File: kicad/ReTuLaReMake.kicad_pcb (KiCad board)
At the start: 2 copper layers, 54 x 26 mm, 23 parts, among them J1 40 Pin DIP Header, U1 ATF1508AS-10AU100

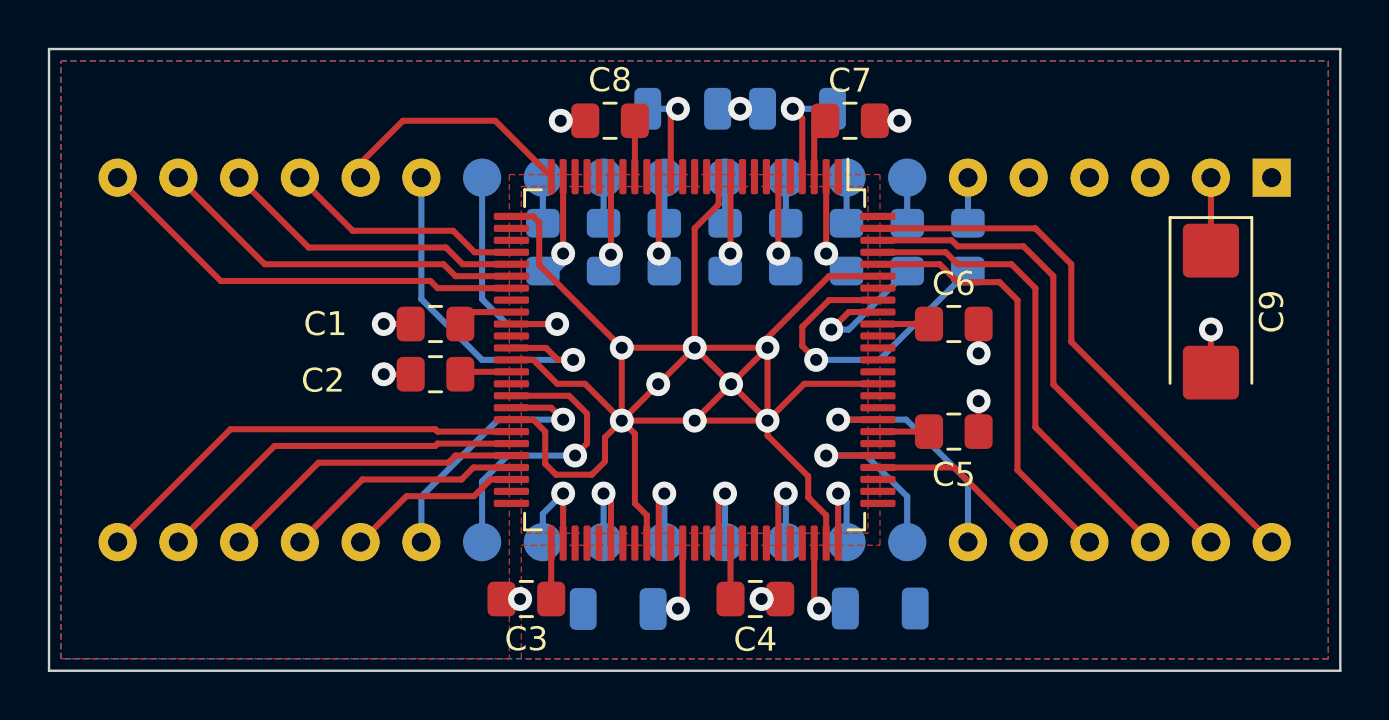
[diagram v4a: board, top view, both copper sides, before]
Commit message: KiCAD: Correct pin assignments to match JK's PCBs
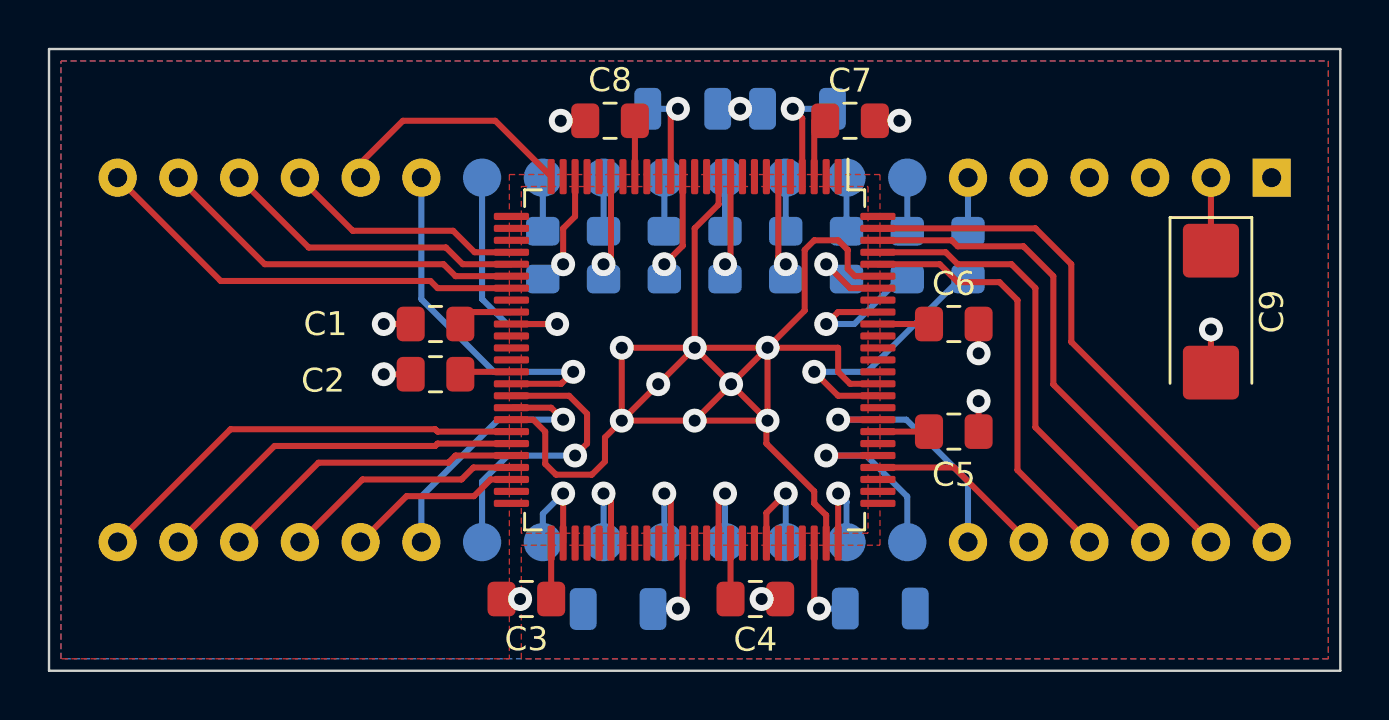
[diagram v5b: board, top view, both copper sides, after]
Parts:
- moved R1 0.33 mm to (138.4, 115.0)
- moved R2 0.33 mm to (135.9, 115.0)
- moved R3 0.33 mm to (133.3, 115.0)
- moved R4 0.33 mm to (130.8, 115.0)
- moved R5 0.33 mm to (128.3, 115.0)
- moved R6 0.33 mm to (125.7, 115.0)
- moved R7 0.33 mm to (123.2, 115.0)
- moved R8 0.33 mm to (120.7, 115.0)
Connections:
- U1 pad 14: unconnected-(U1-Pad14) -> /HD5
- U1 pad 16: /HD5 -> unconnected-(U1-Pad16)
- U1 pad 2: /HD2 -> unconnected-(U1-Pad2)
- U1 pad 23: unconnected-(U1-Pad23) -> /HD7
- U1 pad 24: /HD7 -> unconnected-(U1-Pad24)
- U1 pad 37: /HA1 -> unconnected-(U1-Pad37)
- U1 pad 40: unconnected-(U1-Pad40) -> /HA1
- U1 pad 60: /PD5 -> unconnected-(U1-Pad60)
- U1 pad 61: unconnected-(U1-Pad61) -> /PD5
- U1 pad 69: unconnected-(U1-Pad69) -> /PD3
- U1 pad 70: /PD3 -> unconnected-(U1-Pad70)
- U1 pad 85: unconnected-(U1-Pad85) -> /HD0
- U1 pad 93: /HD0 -> unconnected-(U1-Pad93)
- U1 pad 94: unconnected-(U1-Pad94) -> /HD2
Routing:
- net GND: track 93.8 -> 78.2 mm
- net /HD0: track 13.1 -> 10.8 mm
- net /HD7: track 4.08 -> 4.98 mm
- net /HD3: track 3.66 -> 4.41 mm
- net /HD6: track 3.70 -> 4.41 mm
- net /HD5: track 4.04 -> 4.60 mm

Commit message: KiCAD: Connect unused CPLD pins to GND
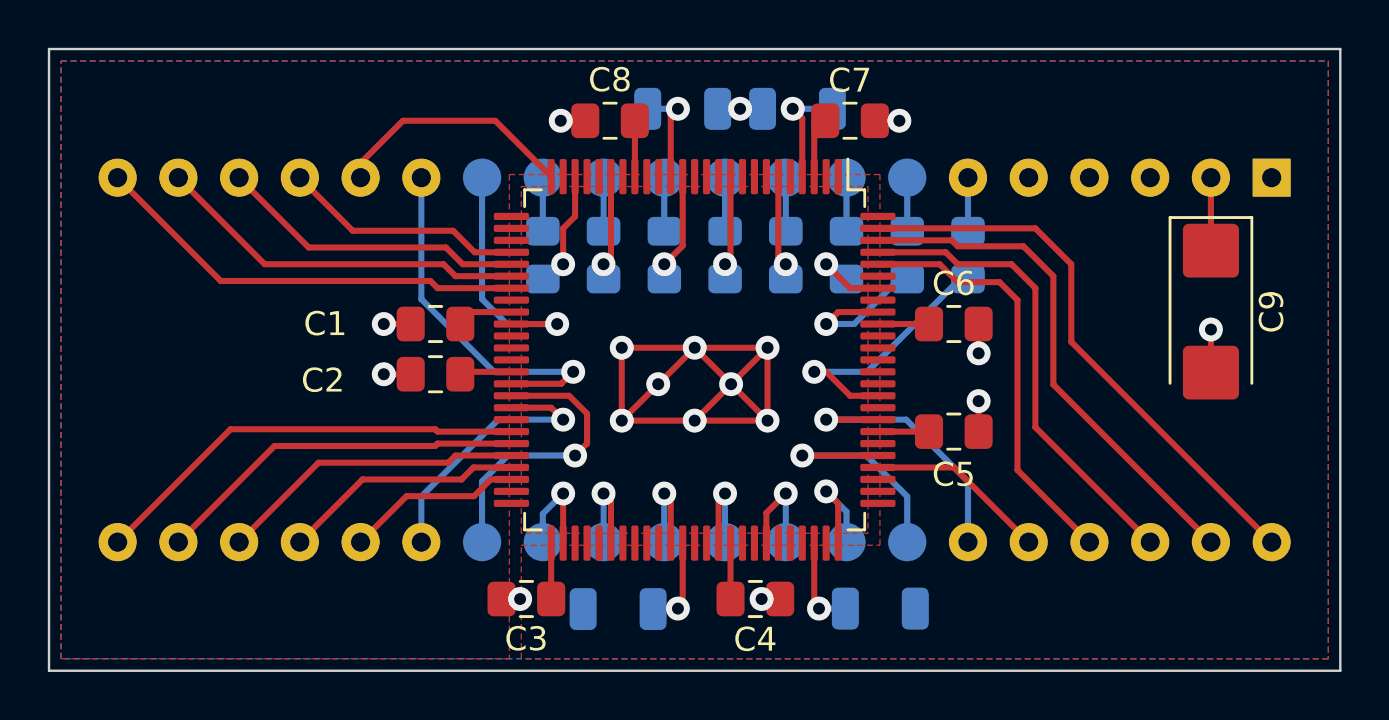
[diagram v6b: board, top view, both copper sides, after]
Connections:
- U1 pad 1: unconnected-(U1-Pad1) -> GND
- U1 pad 100: unconnected-(U1-Pad100) -> GND
- U1 pad 12: unconnected-(U1-Pad12) -> GND
- U1 pad 13: unconnected-(U1-Pad13) -> GND
- U1 pad 16: unconnected-(U1-Pad16) -> GND
- U1 pad 17: unconnected-(U1-Pad17) -> GND
- U1 pad 19: unconnected-(U1-Pad19) -> GND
- U1 pad 2: unconnected-(U1-Pad2) -> GND
- U1 pad 21: unconnected-(U1-Pad21) -> GND
- U1 pad 22: unconnected-(U1-Pad22) -> GND
- U1 pad 24: unconnected-(U1-Pad24) -> GND
- U1 pad 27: unconnected-(U1-Pad27) -> GND
- U1 pad 28: unconnected-(U1-Pad28) -> GND
- U1 pad 33: unconnected-(U1-Pad33) -> GND
- U1 pad 36: unconnected-(U1-Pad36) -> GND
- U1 pad 37: unconnected-(U1-Pad37) -> GND
- U1 pad 49: unconnected-(U1-Pad49) -> GND
- U1 pad 5: unconnected-(U1-Pad5) -> GND
- U1 pad 50: unconnected-(U1-Pad50) -> GND
- U1 pad 53: unconnected-(U1-Pad53) -> GND
- U1 pad 54: unconnected-(U1-Pad54) -> GND
- U1 pad 55: unconnected-(U1-Pad55) -> GND
- U1 pad 57: unconnected-(U1-Pad57) -> GND
- U1 pad 58: unconnected-(U1-Pad58) -> GND
- U1 pad 60: unconnected-(U1-Pad60) -> GND
- U1 pad 63: unconnected-(U1-Pad63) -> GND
- U1 pad 64: unconnected-(U1-Pad64) -> GND
- U1 pad 67: unconnected-(U1-Pad67) -> GND
- U1 pad 68: unconnected-(U1-Pad68) -> GND
- U1 pad 7: unconnected-(U1-Pad7) -> GND
- U1 pad 70: unconnected-(U1-Pad70) -> GND
- U1 pad 71: unconnected-(U1-Pad71) -> GND
- U1 pad 72: unconnected-(U1-Pad72) -> GND
- U1 pad 76: unconnected-(U1-Pad76) -> GND
- U1 pad 77: unconnected-(U1-Pad77) -> GND
- U1 pad 78: unconnected-(U1-Pad78) -> GND
- U1 pad 8: unconnected-(U1-Pad8) -> GND
- U1 pad 81: unconnected-(U1-Pad81) -> GND
- U1 pad 84: unconnected-(U1-Pad84) -> GND
- U1 pad 87: unconnected-(U1-Pad87) -> GND
- U1 pad 88: unconnected-(U1-Pad88) -> GND
- U1 pad 89: unconnected-(U1-Pad89) -> GND
- U1 pad 9: unconnected-(U1-Pad9) -> GND
- U1 pad 90: unconnected-(U1-Pad90) -> GND
- U1 pad 93: unconnected-(U1-Pad93) -> GND
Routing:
- net GND: track 78.2 -> 41.8 mm
- net /PD1: track 8.17 -> 10.2 mm
- net /PD0: track 10.7 -> 11.7 mm
- net /PD2: track 4.25 -> 4.84 mm

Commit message: KiCAD: Rotated CPLD 180 degrees and changed pinout
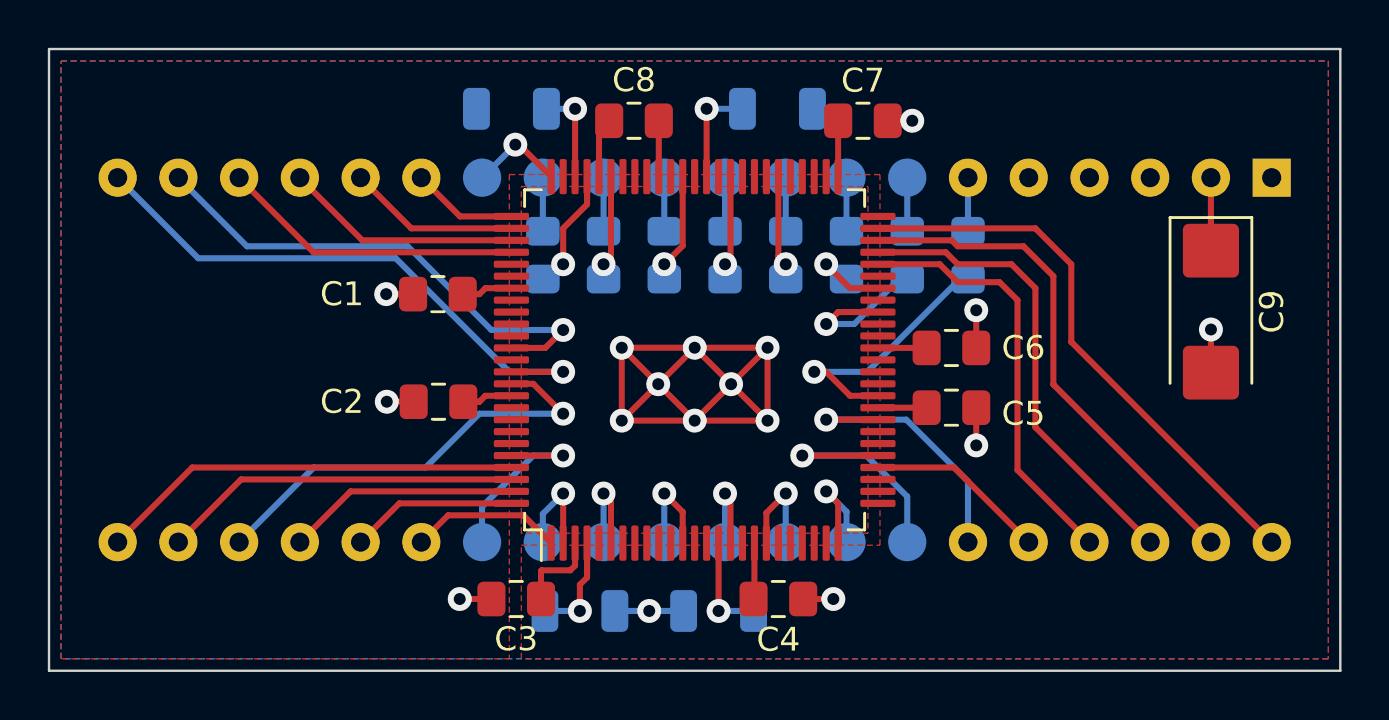
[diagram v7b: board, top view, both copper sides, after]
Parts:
- moved R10 7.16 mm to (119.3, 108.9), turned to 180 degrees
- moved R11 6.76 mm to (128.0, 129.9), turned to 180 degrees
- moved R12 1.60 mm to (122.2, 129.9)
- moved C1 1.25 mm to (116.3, 116.6)
- moved C2 1.16 mm to (116.3, 121.1)
- moved C5 1.00 mm to (137.7, 121.4)
- moved C6 1.00 mm to (137.7, 118.9)
- moved C8 1.00 mm to (124.5, 109.4)
- moved C4 0.96 mm to (130.5, 129.4)
- moved R9 0.84 mm to (130.5, 108.9), turned to 0 degrees
- moved C7 0.54 mm to (134.0, 109.4)
- moved C3 0.43 mm to (119.5, 129.4)
- turned U1 to 90 degrees
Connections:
- R10 pad 1: Net-(R10-Pad1) -> Net-(U1-Pad73)
- R10 pad 2: VCC -> unconnected-(R10-Pad2)
- R11 pad 2: unconnected-(R11-Pad2) -> VCC
- R12 pad 1: Net-(R12-Pad1) -> VCC
- R12 pad 2: GND -> Net-(R12-Pad2)
- R9 pad 1: Net-(R9-Pad1) -> Net-(U1-Pad62)
- R9 pad 2: VCC -> GND
- U1 pad 1: GND -> /PA1
- U1 pad 10: /HD4 -> GND
- U1 pad 100: GND -> /PA2
- U1 pad 12: GND -> /PD5
- U1 pad 14: /HD5 -> GND
- U1 pad 15: Net-(R10-Pad1) -> Net-(R11-Pad1)
- U1 pad 16: GND -> /PD4
- U1 pad 19: GND -> /PD3
- U1 pad 2: GND -> /PD7
- U1 pad 20: /HD6 -> GND
- U1 pad 23: /HD7 -> GND
- U1 pad 25: /HA2 -> /PD2
- U1 pad 29: /HRnW -> /PIRQ
- U1 pad 30: /HCS -> /PD1
- U1 pad 31: /HO2 -> GND
- U1 pad 32: /HRST -> GND
- U1 pad 33: GND -> /PD0
- U1 pad 35: /HA0 -> /HD0
- U1 pad 4: Net-(R9-Pad1) -> Net-(R12-Pad2)
- U1 pad 40: /HA1 -> GND
- U1 pad 41: /PA0 -> GND
- U1 pad 42: /PA1 -> /HD1
- U1 pad 44: /PCS -> /HD2
- U1 pad 45: /PNRDS -> GND
- U1 pad 46: /PNWDS -> /PRST
- U1 pad 47: /DACK -> /DRQ
- U1 pad 48: /PA2 -> /HIRQ
- U1 pad 49: GND -> /PNMI
- U1 pad 52: /PD7 -> GND
- U1 pad 56: /PD6 -> /HD3
- U1 pad 6: /HD3 -> /PD6
- U1 pad 60: GND -> /HD4
- U1 pad 61: /PD5 -> GND
- U1 pad 62: Net-(R12-Pad1) -> Net-(U1-Pad62)
- U1 pad 64: GND -> /HD5
- U1 pad 65: /PD4 -> GND
- U1 pad 69: /PD3 -> GND
- U1 pad 70: GND -> /HD6
- U1 pad 72: GND -> /HD7
- U1 pad 73: Net-(R11-Pad1) -> Net-(U1-Pad73)
- U1 pad 75: /PD2 -> /HA0
- U1 pad 76: GND -> /HA1
- U1 pad 77: GND -> /HA2
- U1 pad 78: GND -> /HRnW
- U1 pad 79: /PIRQ -> /HCS
- U1 pad 80: /PD1 -> GND
- U1 pad 83: /PD0 -> GND
- U1 pad 85: /HD0 -> GND
- U1 pad 87: GND -> /HO2
- U1 pad 89: GND -> /HRST
- U1 pad 90: GND -> /PNWDS
- U1 pad 92: /HD1 -> GND
- U1 pad 94: /HD2 -> GND
- U1 pad 96: /PRST -> /PA0
- U1 pad 97: /DRQ -> /PCS
- U1 pad 98: /HIRQ -> /PNRDS
- U1 pad 99: /PNMI -> /DACK
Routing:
- net /HA1: track 15.5 -> 4.44 mm, vias 1 -> 0
- net GND: track 41.8 -> 48.6 mm, vias 17 -> 16
- net /HA0: track 10.6 -> 4.01 mm
- net /HRST: track 18.4 -> 24.2 mm, vias 0 -> 1
- net /HO2: track 15.6 -> 21.2 mm, vias 0 -> 1
- net /PNWDS: track 12.9 -> 18.5 mm, vias 0 -> 1
- net /PA1: track 11.5 -> 6.38 mm, vias 1 -> 0
- net Net-(R9-Pad1): track 4.67 -> 0.00 mm, vias 1 -> 0
- net Net-(R12-Pad2): track 0.00 -> 4.42 mm, vias 0 -> 1
- net /PA0: track 12.3 -> 7.92 mm
- net Net-(U1-Pad62): track 0.00 -> 4.34 mm, vias 0 -> 1
- net Net-(R10-Pad1): track 4.22 -> 0.00 mm, vias 1 -> 0
- net Net-(U1-Pad73): track 0.00 -> 4.04 mm, vias 0 -> 1
- net Net-(R12-Pad1): track 3.84 -> 0.00 mm, vias 1 -> 0
- net /HA2: track 9.68 -> 7.19 mm
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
